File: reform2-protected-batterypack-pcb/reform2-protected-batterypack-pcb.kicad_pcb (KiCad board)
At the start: 2 copper layers, 91 x 66 mm, 38 parts, among them J1 Conn_01x05_Female, Q1 PMV50ENEAR, Q2 PMV50ENEAR, Q3 PMV50ENEAR, Q4 PMV50ENEAR, Q5 PMV50ENEAR, Q6 PMV50ENEAR, Q7 PMV50ENEAR, Q8 PMV50ENEAR, U1 KEYSTONE_54, U2 KEYSTONE_54, U3 KEYSTONE_54, U4 KEYSTONE_54, U5 R5617x, U6 R5617x, U7 R5617x, U8 R5617x

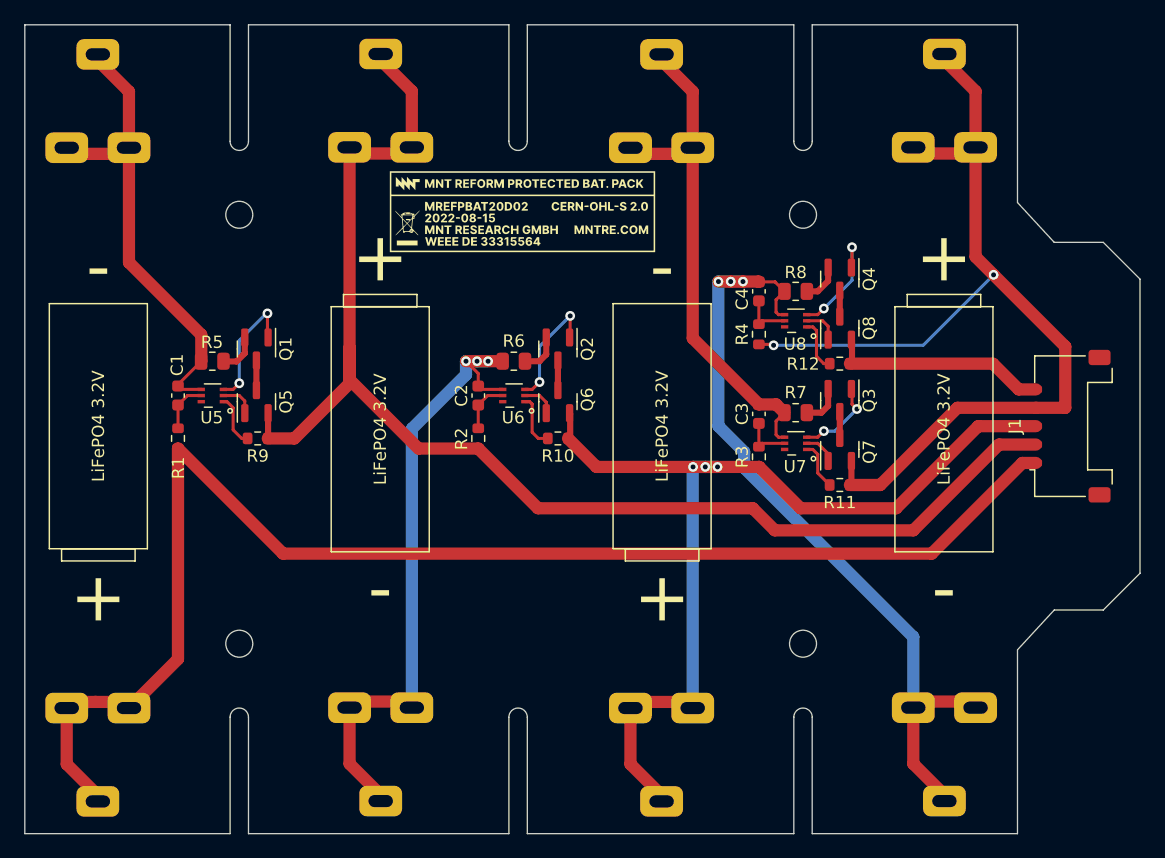
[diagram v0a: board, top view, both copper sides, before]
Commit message: protected battery pack: add release candidate
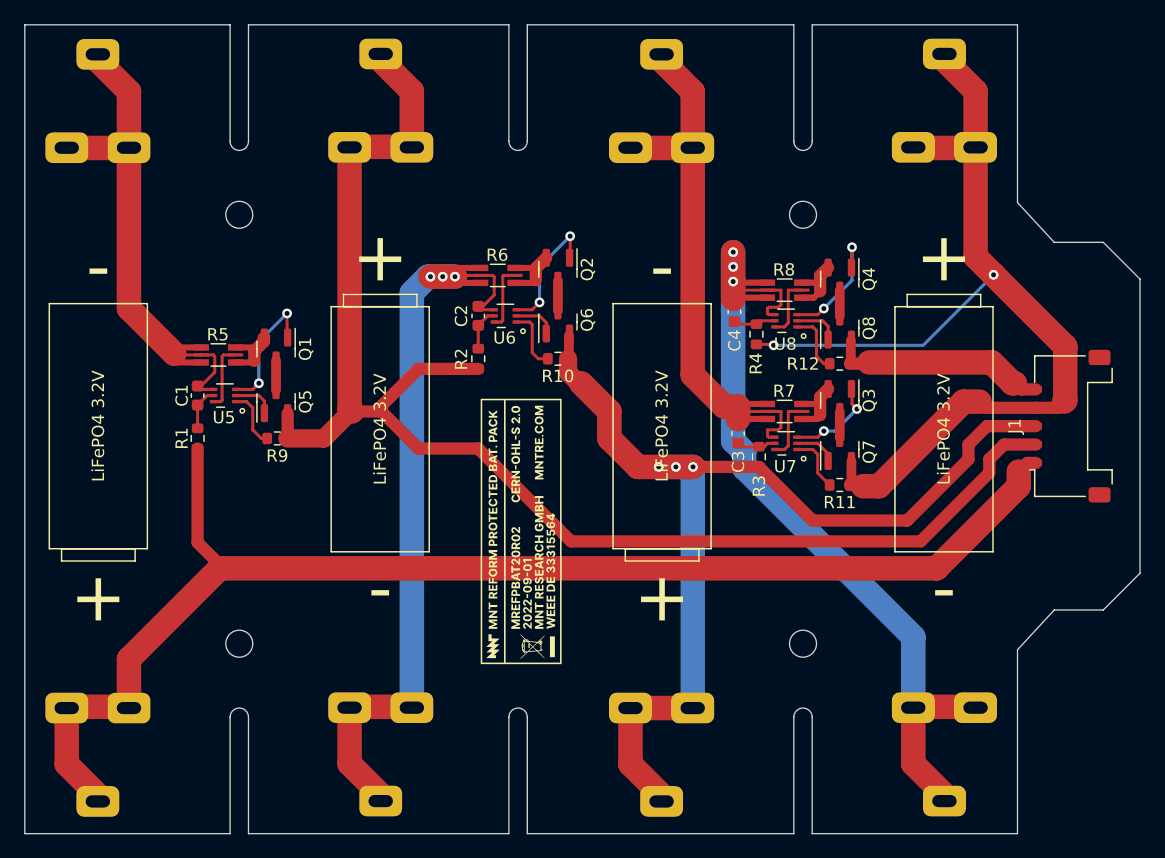
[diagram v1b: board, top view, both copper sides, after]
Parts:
- R5, R6, R7, R8: footprint Resistor_SMD:R_0805_2012Metric -> footprints:R_1206_3216Metric_Kelvin
- moved H1 26.1 mm to (97.5, 102.1), turned to 90 degrees
- moved R6 7.12 mm to (95.6, 81.2)
- moved U6 6.54 mm to (96.2, 84.5)
- moved C2 6.50 mm to (94.0, 84.5)
- moved Q2 6.50 mm to (100.5, 80.7)
- moved Q6 6.50 mm to (100.5, 85.0)
- moved R10 6.50 mm to (100.5, 88.0)
- moved R2 6.50 mm to (94.0, 88.0)
- moved C4 2.61 mm to (114.9, 84.2)
- moved C3 2.33 mm to (115.2, 94.1)
- moved C1 1.60 mm to (71.1, 91.0)
- moved Q1 1.60 mm to (77.5, 87.2)
- moved Q5 1.60 mm to (77.5, 91.5)
- moved R1 1.60 mm to (71.1, 94.5)
- moved R9 1.60 mm to (77.6, 94.5)
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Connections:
- R5 pad 2: Net-(Q1-Pad2) -> Net-(C1-Pad1)
- R6 pad 2: Net-(Q2-Pad2) -> Net-(C2-Pad1)
- R7 pad 2: Net-(Q3-Pad2) -> Net-(C3-Pad1)
- R8 pad 2: Net-(Q4-Pad2) -> Net-(C4-Pad1)
- U5 pad 6: Net-(Q1-Pad2) -> Net-(U5-Pad6)
- U6 pad 6: Net-(Q2-Pad2) -> Net-(R6-Pad3)
- U7 pad 6: Net-(Q3-Pad2) -> Net-(R7-Pad3)
- U8 pad 6: Net-(Q4-Pad2) -> Net-(R8-Pad3)
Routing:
- net Net-(C2-Pad1): track 53.2 -> 65.8 mm
- net Net-(C4-Pad1): track 65.6 -> 73.4 mm
- net Net-(C1-Pad1): track 38.4 -> 46.0 mm
- net Net-(C3-Pad1): track 42.2 -> 49.3 mm
- net /V4: track 110.2 -> 116.8 mm
- net /V3: track 80.9 -> 86.7 mm
- net Net-(U5-Pad6): track 0.00 -> 5.48 mm
- net Net-(R6-Pad3): track 0.00 -> 5.40 mm
- net Net-(R7-Pad3): track 0.00 -> 5.12 mm
- net Net-(R8-Pad3): track 0.00 -> 5.01 mm
- net /V5: track 113.2 -> 108.7 mm
- net Net-(Q3-Pad2): track 3.35 -> 6.61 mm
- net Net-(Q1-Pad2): track 3.25 -> 6.33 mm
- net Net-(Q4-Pad2): track 3.18 -> 5.51 mm
- net Net-(Q2-Pad2): track 3.35 -> 5.39 mm
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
